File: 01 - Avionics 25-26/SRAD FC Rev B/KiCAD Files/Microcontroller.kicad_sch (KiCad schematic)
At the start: 4 parts

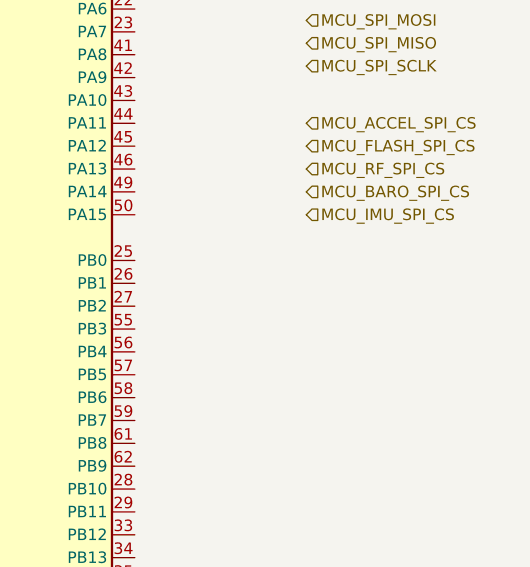
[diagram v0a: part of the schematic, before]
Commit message: wired gps uart
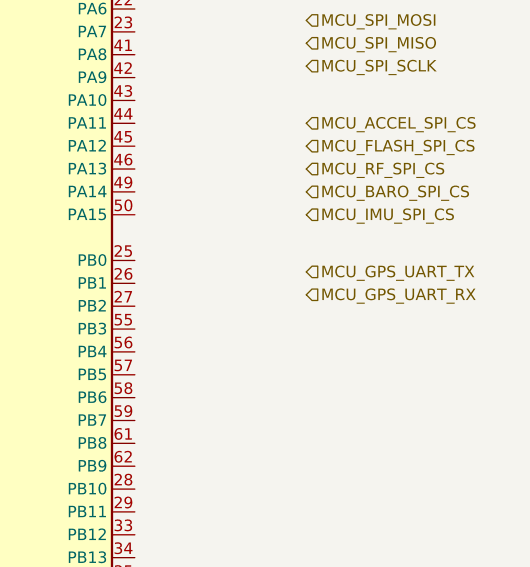
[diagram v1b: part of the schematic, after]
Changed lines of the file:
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@@
+		)
+	)
+	(hierarchical_label "MCU_GPS_UART_TX"
+		(shape input)
+		(at 160.02 97.79 0)
+		(effects
+			(font
+				(size 1.27 1.27)
+			)
+			(justify left)
 		)
 	)
@@
 		(effects
 			(font
+				(size 1.27 1.27)
+			)
+			(justify left)
+		)
+	)
+	(hierarchical_label "MCU_GPS_UART_RX"
+		(shape input)
+		(at 160.02 100.33 0)
+		(effects
+			(font

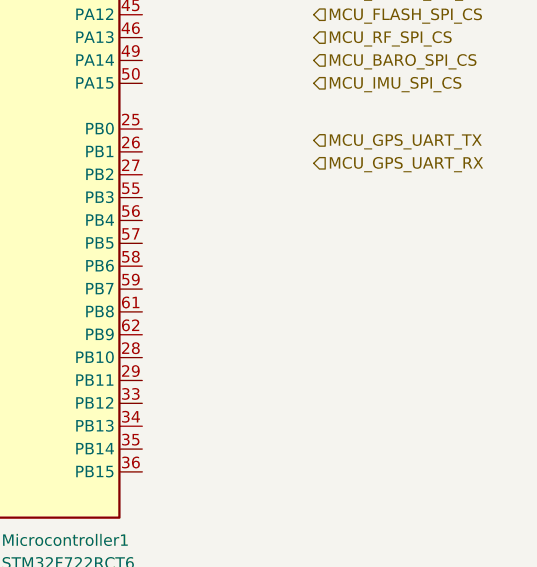
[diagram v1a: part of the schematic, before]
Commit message: wired interrupt sources
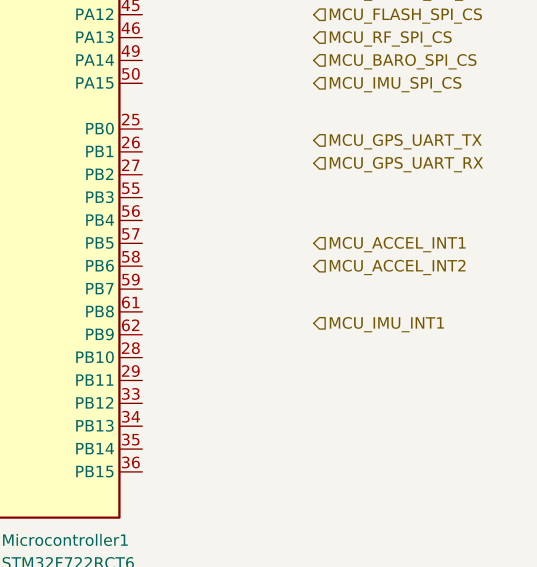
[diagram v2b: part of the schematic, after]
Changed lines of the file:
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@@
+		)
+	)
+	(hierarchical_label "MCU_IMU_INT1"
+		(shape input)
+		(at 160.02 118.11 0)
+		(effects
+			(font
+				(size 1.27 1.27)
+			)
+			(justify left)
 		)
 	)
@@
 		)
 	)
+	(hierarchical_label "MCU_ACCEL_INT2"
+		(shape input)
+		(at 160.02 111.76 0)
+		(effects
+			(font
+				(size 1.27 1.27)
+			)
+			(justify left)
+		)
+	)
 	(hierarchical_label "MCU_RF_SPI_CS"
 		(shape input)
@@
 		(effects
 			(font
+				(size 1.27 1.27)
+			)
+			(justify left)
+		)
+	)
+	(hierarchical_label "MCU_ACCEL_INT1"
+		(shape input)
+		(at 160.02 109.22 0)
+		(effects
+			(font

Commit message: moved..... stuff
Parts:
- added J1: Conn_ARM_SWD_TagConnect_TC2030, Connector:Tag-Connect_TC2030-IDC-FP_2x03_P1.27mm_Vertical, symbol Connector:Conn_ARM_SWD_TagConnect_TC2030
- added Reset_Swtich: SW_Push, symbol Switch:SW_Push
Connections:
- net NRST: no longer names the net of Microcontroller1.7 (NRST)
- net NRST: now also J1.3 (~{RESET}), Reset_Swtich.1
- net STLINK_JTCK_SWCLK: no longer names the net of Microcontroller1.3 (PC14)
- net STLINK_JTCK_SWCLK: now also J1.4 (SWCLK)
- net STLINK_JTMS_SWDIO: no longer names the net of Microcontroller1.2 (PC13)
- net STLINK_JTMS_SWDIO: now also J1.2 (SWDIO)
- new net GND: J1.5 (GND), Reset_Swtich.2
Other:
- note added: "WIRE ME"
- moved on the sheet: C3, R1, R2

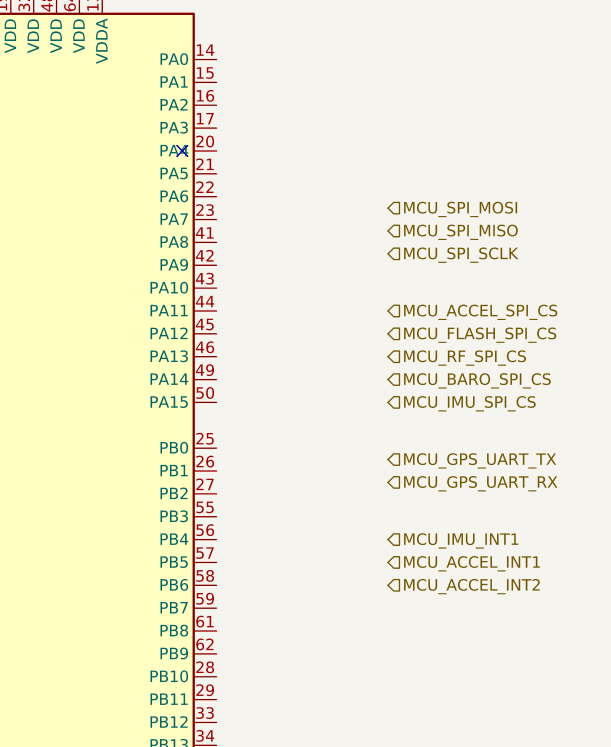
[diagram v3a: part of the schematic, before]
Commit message: wired microcontroller pins
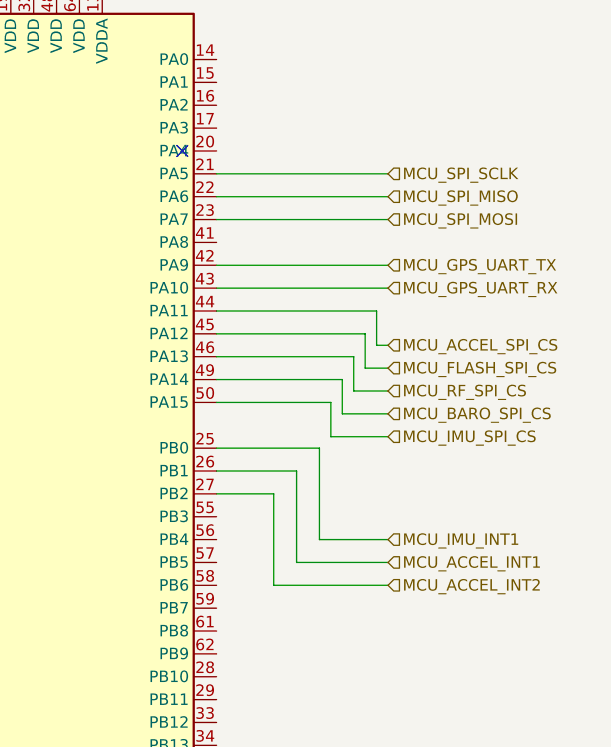
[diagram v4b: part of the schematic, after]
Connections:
- net MCU_ACCEL_INT1: now also Microcontroller1.26 (PB1)
- net MCU_ACCEL_INT2: now also Microcontroller1.27 (PB2)
- net MCU_ACCEL_SPI_CS: now also Microcontroller1.44 (PA11)
- net MCU_BARO_SPI_CS: now also Microcontroller1.49 (PA14)
- net MCU_FLASH_SPI_CS: now also Microcontroller1.45 (PA12)
- net MCU_GPS_UART_RX: now also Microcontroller1.43 (PA10)
- net MCU_GPS_UART_TX: now also Microcontroller1.42 (PA9)
- net MCU_IMU_INT1: now also Microcontroller1.25 (PB0)
- net MCU_IMU_SPI_CS: now also Microcontroller1.50 (PA15)
- net MCU_RF_SPI_CS: now also Microcontroller1.46 (PA13)
- net MCU_SPI_MISO: now also Microcontroller1.22 (PA6)
- net MCU_SPI_MOSI: now also Microcontroller1.23 (PA7)
- net MCU_SPI_SCLK: now also Microcontroller1.21 (PA5)

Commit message: general fixes for sheet sheet, ERC error fixes
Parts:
- renumbered C3 to C103, R1 to R101, R2 to R13, Reset_Swtich to Reset_Swtich1
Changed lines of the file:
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@@
 		(dnp no)
 		(fields_autoplaced yes)
-		(property "Reference" "R2"
+		(property "Reference" "R13"
 			(at 85.09 130.81 90)
 			(effects
@@
 			(project ""
 				(path "/1dd9e63a-24f2-43c6-ae21-66b89e6998f2/9bb21508-08d3-4d29-a04f-971573e7774c"
-					(reference "R2")
+					(reference "R13")
 					(unit 1)
 				)
@@
 		(dnp no)
 		(fields_autoplaced yes)
-		(property "Reference" "R1"
+		(property "Reference" "R101"
 			(at 72.39 119.38 90)
 			(effects
@@
 			(project ""
 				(path "/1dd9e63a-24f2-43c6-ae21-66b89e6998f2/9bb21508-08d3-4d29-a04f-971573e7774c"
-					(reference "R1")
+					(reference "R101")
 					(unit 1)
 				)
@@
 		(dnp no)
 		(fields_autoplaced yes)
-		(property "Reference" "Reset_Swtich"
+		(property "Reference" "Reset_Swtich1"
 			(at 90.17 25.4 0)
 			(effects
@@
 			(project "SRAD FC Rev B"
 				(path "/1dd9e63a-24f2-43c6-ae21-66b89e6998f2/9bb21508-08d3-4d29-a04f-971573e7774c"
-					(reference "Reset_Swtich")
+					(reference "Reset_Swtich1")
 					(unit 1)
 				)
@@
 		(dnp no)
 		(fields_autoplaced yes)
-		(property "Reference" "C3"
+		(property "Reference" "C103"
 			(at 85.09 118.11 90)
 			(effects
@@
 			(project ""
 				(path "/1dd9e63a-24f2-43c6-ae21-66b89e6998f2/9bb21508-08d3-4d29-a04f-971573e7774c"
-					(reference "C3")
-					(unit 1)
-				)
+					(reference "C103")
+					(unit 1)
+				)

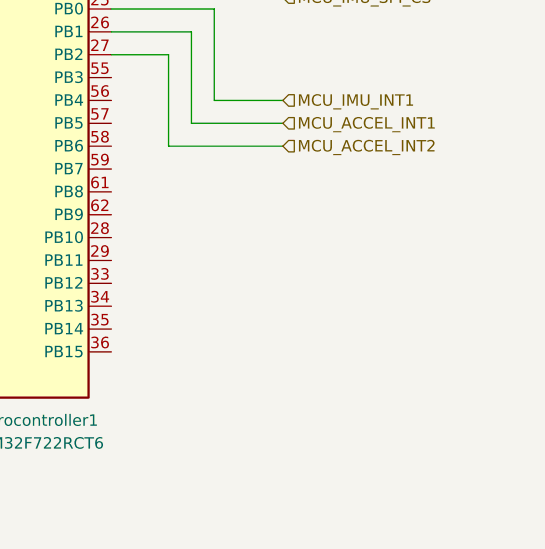
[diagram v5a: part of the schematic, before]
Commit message: wired pyro to the mcu in top level sheet
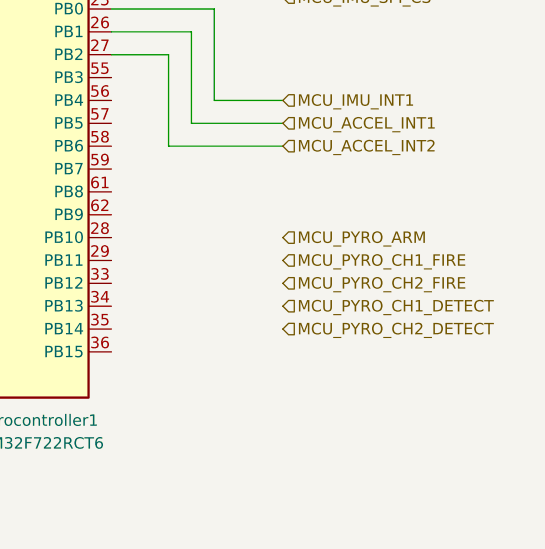
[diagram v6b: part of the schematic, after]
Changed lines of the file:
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@@
+		)
+	)
+	(hierarchical_label "MCU_PYRO_CH1_DETECT"
+		(shape input)
+		(at 160.02 129.54 0)
+		(effects
+			(font
+				(size 1.27 1.27)
+			)
+			(justify left)
 		)
 	)
@@
 		)
 	)
+	(hierarchical_label "MCU_PYRO_CH2_FIRE"
+		(shape input)
+		(at 160.02 127 0)
+		(effects
+			(font
+				(size 1.27 1.27)
+			)
+			(justify left)
+		)
+	)
 	(hierarchical_label "VSSA"
 		(shape input)
@@
 		)
 	)
+	(hierarchical_label "MCU_PYRO_ARM"
+		(shape input)
+		(at 160.02 121.92 0)
+		(effects
+			(font
+				(size 1.27 1.27)
+			)
+			(justify left)
+		)
+	)
 	(hierarchical_label "BOOT0"
 		(shape input)
@@
 		)
 	)
+	(hierarchical_label "MCU_PYRO_CH1_FIRE"
+		(shape input)
+		(at 160.02 124.46 0)
+		(effects
+			(font
+				(size 1.27 1.27)
+			)
+			(justify left)
+		)
+	)
+	(hierarchical_label "MCU_PYRO_CH2_DETECT"
+		(shape input)
+		(at 160.02 132.08 0)
+		(effects
+			(font
+				(size 1.27 1.27)
+			)
+			(justify left)
+		)
+	)

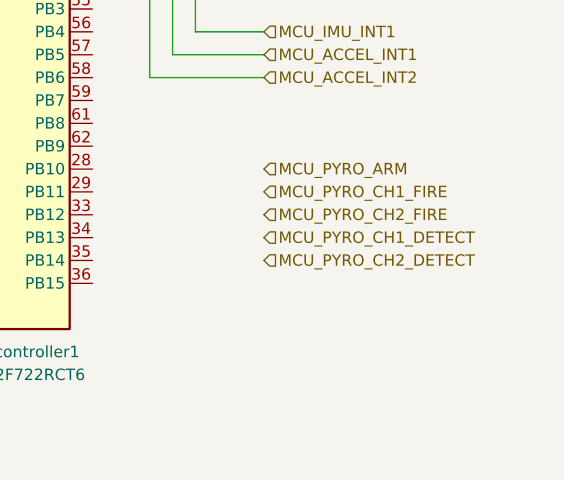
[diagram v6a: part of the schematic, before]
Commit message: wired pyro current sense, rearranged some stuff
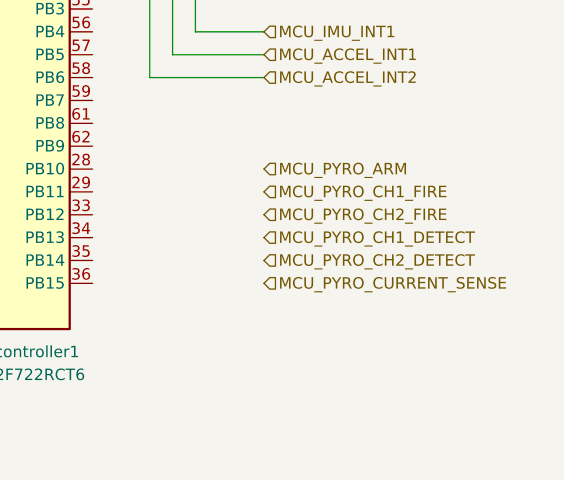
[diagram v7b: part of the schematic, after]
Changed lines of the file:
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@@
+		)
+	)
+	(hierarchical_label "MCU_PYRO_CURRENT_SENSE"
+		(shape input)
+		(at 160.02 134.62 0)
+		(effects
+			(font
+				(size 1.27 1.27)
+			)
+			(justify left)
 		)
 	)

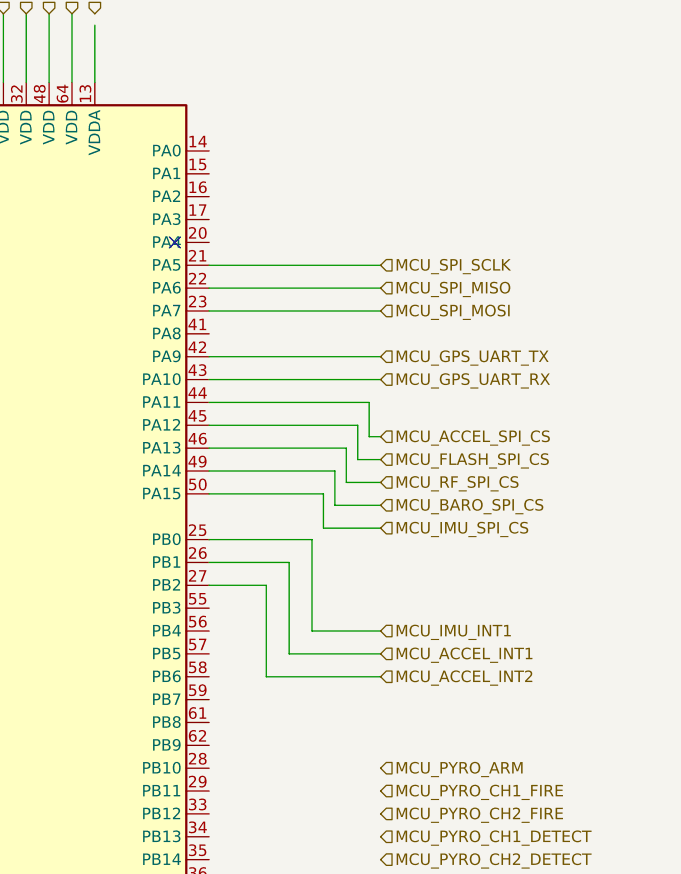
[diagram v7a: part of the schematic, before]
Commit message: added some more wiring for GPS
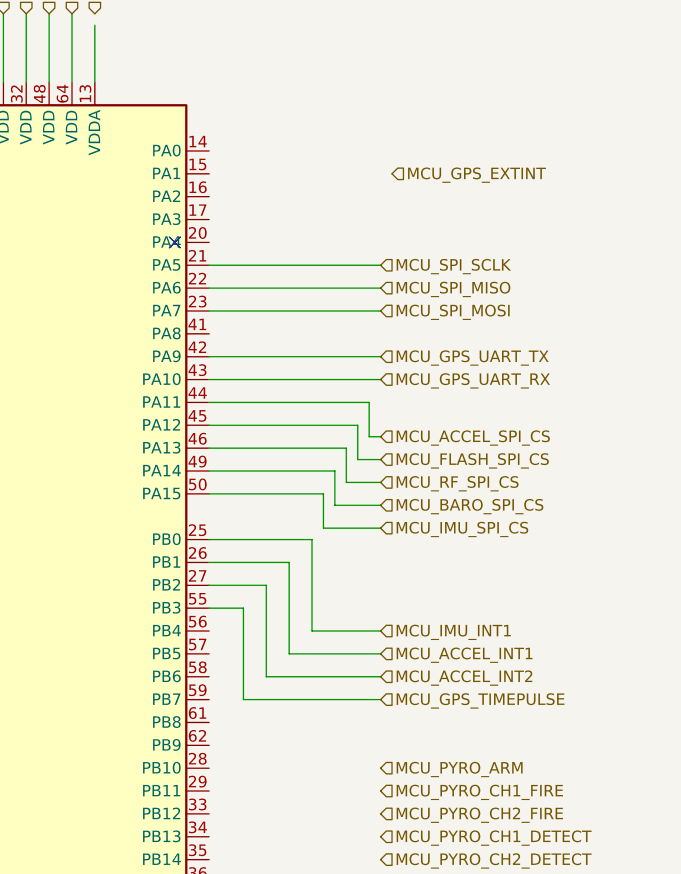
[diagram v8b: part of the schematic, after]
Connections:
- net MCU_GPS_TIMEPULSE: now reaches Microcontroller1.55 (PB3)
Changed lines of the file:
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@@
+	(wire
+		(pts
+			(xy 144.78 114.3) (xy 144.78 104.14)
+		)
+		(stroke
+			(width 0)
+			(type default)
+		)
+	)
 	(wire
 		(pts
@@
 	(wire
 		(pts
+			(xy 160.02 114.3) (xy 144.78 114.3)
+		)
+		(stroke
+			(width 0)
+			(type default)
+		)
+	)
+	(wire
+		(pts
 			(xy 92.71 58.42) (xy 100.33 58.42)
 		)
@@
 	(wire
 		(pts
+			(xy 144.78 104.14) (xy 140.97 104.14)
+		)
+		(stroke
+			(width 0)
+			(type default)
+		)
+	)
+	(wire
+		(pts
 			(xy 160.02 90.17) (xy 156.21 90.17)
 		)
@@
 		)
 	)
+	(hierarchical_label "MCU_GPS_EXTINT"
+		(shape input)
+		(at 161.29 55.88 0)
+		(effects
+			(font
+				(size 1.27 1.27)
+			)
+			(justify left)
+		)
+	)
 	(hierarchical_label "MCU_FLASH_SPI_CS"
 		(shape input)
@@
 		(effects
 			(font
+				(size 1.27 1.27)
+			)
+			(justify left)
+		)
+	)
+	(hierarchical_label "MCU_GPS_TIMEPULSE"
+		(shape input)
+		(at 160.02 114.3 0)
+		(effects
+			(font
